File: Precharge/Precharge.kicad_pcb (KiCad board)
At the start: 2 copper layers, 85 x 85 mm, 70 parts, among them J1 Conn_01x02, J2 Conn_01x02, J3 Molex MicroFit, J4 Conn_02x03_Counter_Clockwise, K1 KT12-1A-40L-THT, Q1 CJ2310, Q2 AO3400A, Q3 AO3400A, U1 LM393, U3 4N35, U4 4N35

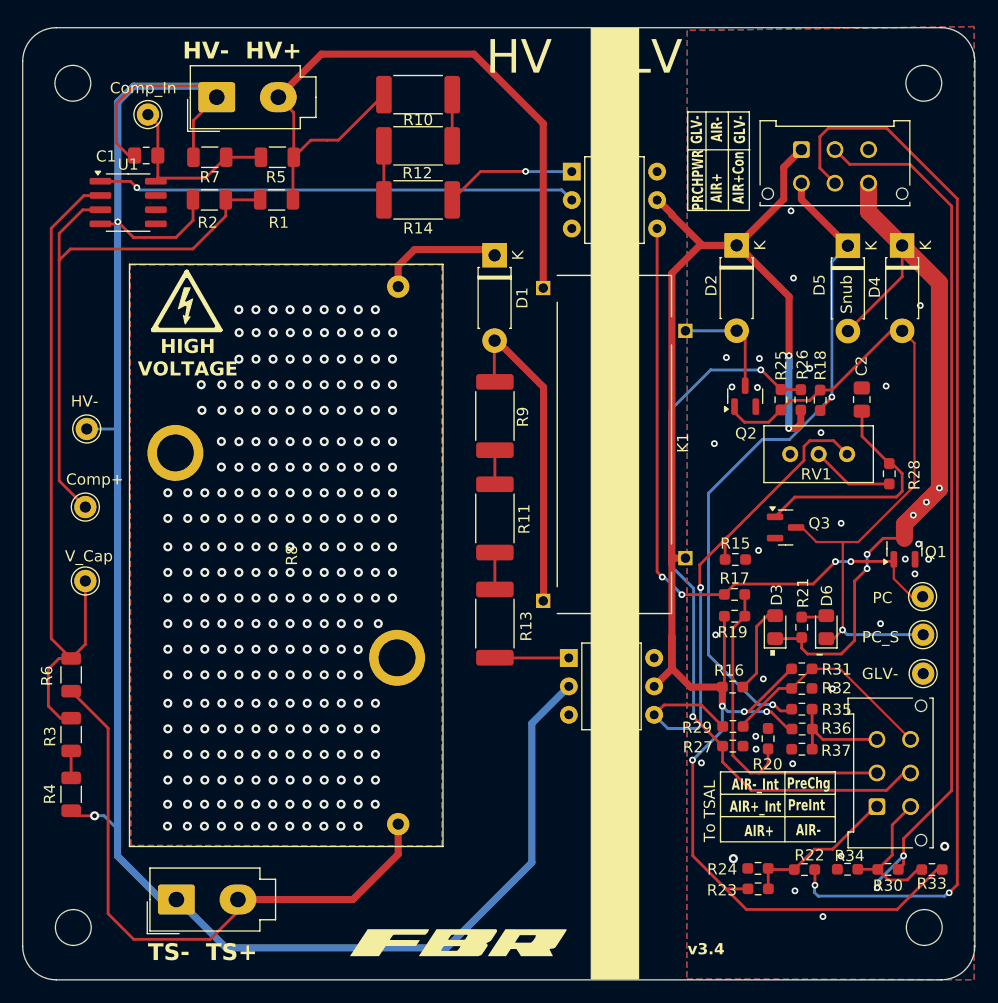
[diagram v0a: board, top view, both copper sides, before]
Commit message: Precharge: Add isolated DC-DC
New Precharge version
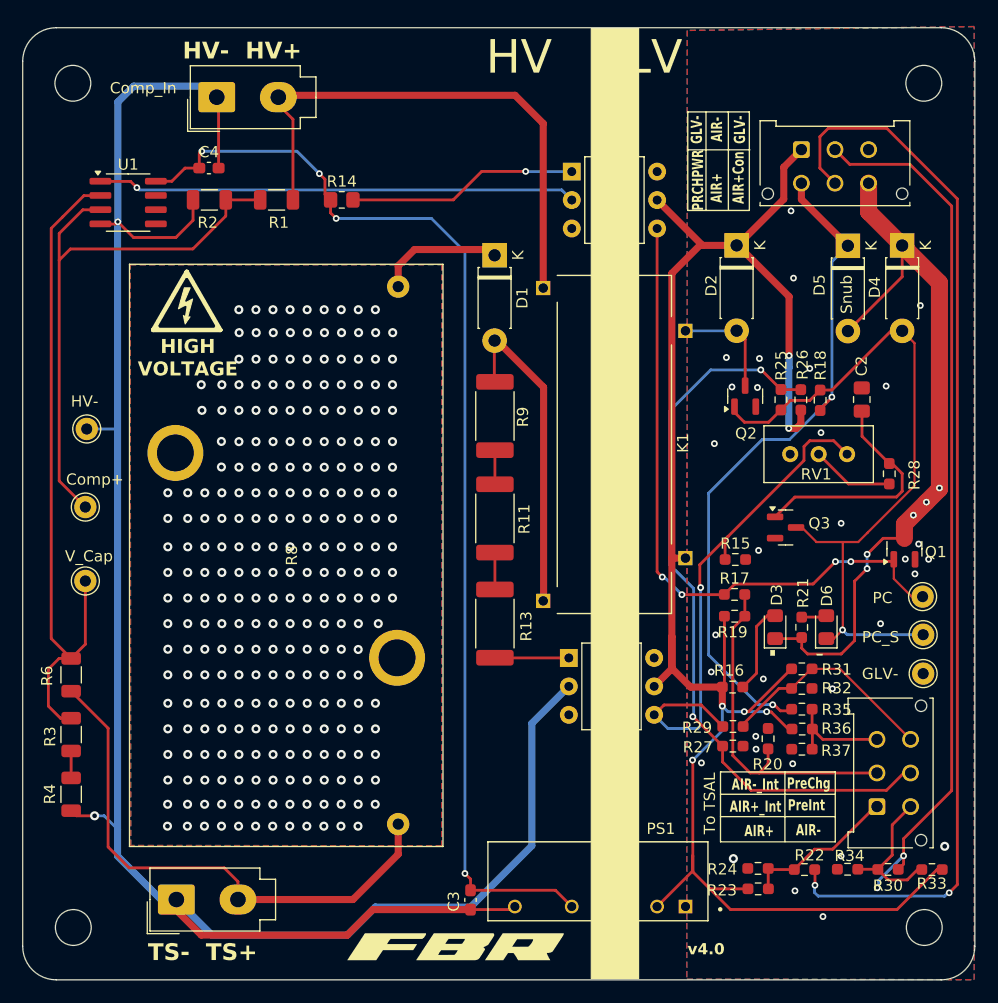
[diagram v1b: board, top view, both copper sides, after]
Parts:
- removed C1: 0.1 uF, Capacitor_SMD:C_0805_2012Metric_Pad1.18x1.45mm_HandSolder
- removed R10, R12: 3.3K, Resistor_SMD:R_2512_6332Metric_Pad1.40x3.35mm_HandSolder
- removed R5: 15K, Resistor_SMD:R_1206_3216Metric
- removed R7: 1.5K, Resistor_SMD:R_1206_3216Metric
- removed TP4: TestPoint, Connector_Pin:Pin_D1.0mm_L10.0mm
- added C3: 0.1uF, Capacitor_SMD:C_0603_1608Metric_Pad1.08x0.95mm_HandSolder, F.Cu at (110.9, 129.6)
- added C4: 0.1uF, Capacitor_SMD:C_0603_1608Metric_Pad1.08x0.95mm_HandSolder, F.Cu at (87.5, 64.2)
- added PS1: RKZE-1205S_HP, Recom DC-DC:CONV_RKZE-1205S_HP, F.Cu at (122.2, 127.9)
- R14: value 3.3K -> 330; footprint Resistor_SMD:R_2512_6332Metric_Pad1.40x3.35mm_HandSolder -> Resistor_SMD:R_0805_2012Metric_Pad1.20x1.40mm_HandSolder
- moved R14 6.82 mm to (99.4, 67.1)
- moved G*** 0.44 mm to (109.4, 133.7)
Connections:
- net /AIR+_GND renamed /AIR-_GND
- net /Comp_Out renamed Net-(U1-Pad1)
- net HV+ renamed TS+
- J3 pad 2: /AIR-_Out -> /AIR+_Out
- J3 pad 5: /AIR+_Out -> /AIR-_Out
- J4 pad 1: /AIR+ -> /AIR-
- J4 pad 2: /AIR+_Int -> /AIR-_Int
- J4 pad 3: /AIR-_Int -> /AIR+_Int
- J4 pad 4: /AIR- -> /AIR+
- R14 pad 1: Net-(R12-Pad2) -> /5V+_Iso
- R17 pad 2: /AIR+_Int -> /AIR-_Int
- R19 pad 2: /AIR+_Int -> /AIR-_Int
- R20 pad 1: /AIR+_Int -> /AIR-_Int
- R22 pad 1: /AIR+_Out -> /AIR-_Out
- R22 pad 2: /AIR+ -> /AIR-
- R23 pad 2: /AIR+ -> /AIR-
- R24 pad 1: /AIR+ -> /AIR-
- R30 pad 1: /AIR-_Out -> /AIR+_Out
- R30 pad 2: /AIR- -> /AIR+
- R33 pad 2: /AIR- -> /AIR+
- R34 pad 1: /AIR- -> /AIR+
- R35 pad 2: /AIR-_Int -> /AIR+_Int
- R36 pad 2: /AIR-_Int -> /AIR+_Int
- R37 pad 1: /AIR-_Int -> /AIR+_Int
- U1 pad 8: Net-(U1C-V+) -> /5V+_Iso
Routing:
- net /5V+_Iso: track 0.00 -> 101.6 mm, vias 0 -> 4
- net /AIR-_Int: track 9.99 -> 30.8 mm
- net /AIR+_Int: track 30.8 -> 9.99 mm
- net /AIR-_Out: track 77.8 -> 96.6 mm
- net /AIR+_Out: track 96.6 -> 77.8 mm
- net HV-: track 179.7 -> 196.4 mm
- net Net-(U1C-V+): track 16.0 -> 0.00 mm
- net TS+: track 63.0 -> 49.5 mm
- net Net-(R14-Pad2): track 11.7 -> 20.6 mm
- net GLV+: track 155.2 -> 163.3 mm
- net Net-(J2-Pin_2): track 54.6 -> 49.5 mm
- net Net-(R12-Pad2): track 4.83 -> 0.00 mm
- net Net-(R10-Pad1): track 4.57 -> 0.00 mm
- net /AIR-: track 13.3 -> 14.1 mm
- net /AIR+: track 14.1 -> 13.3 mm
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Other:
- board text added: "v4.0"
- board text removed: "v3.4"

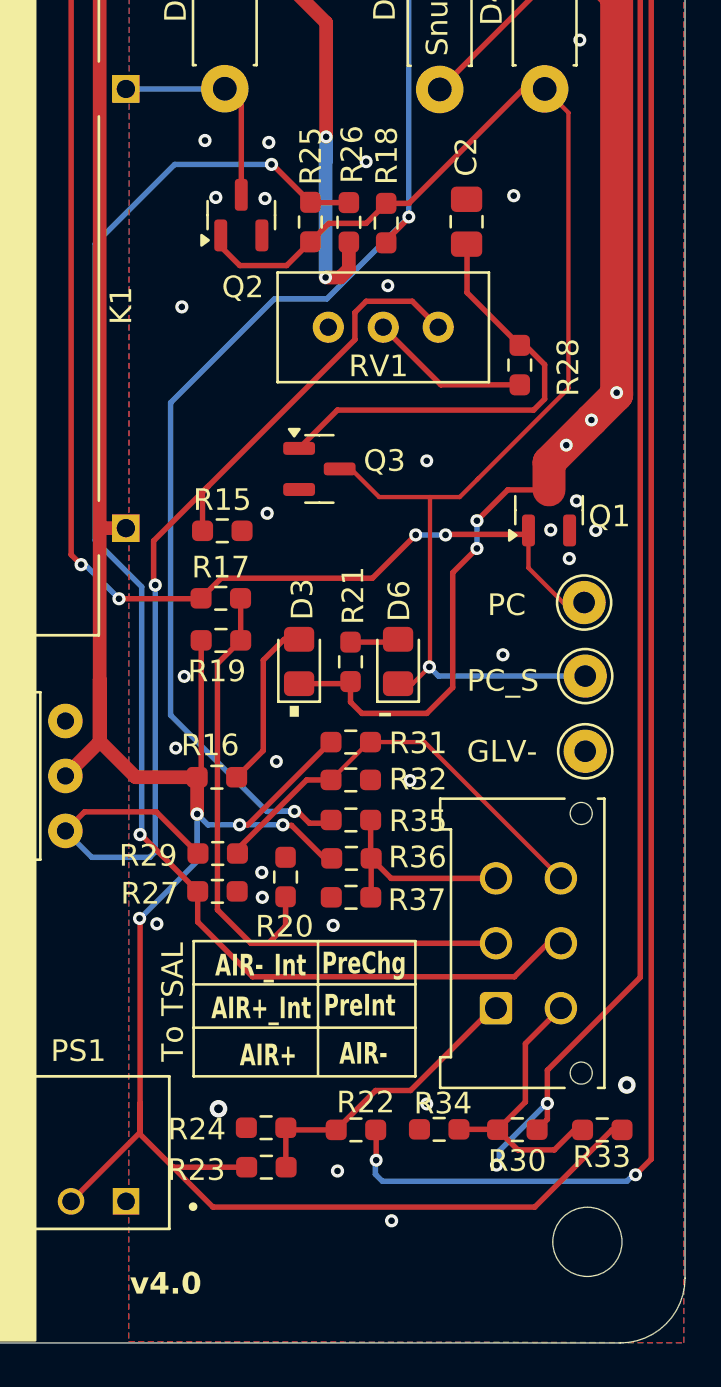
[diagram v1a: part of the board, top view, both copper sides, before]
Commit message: Precharge: cap DC bias correction, PDs on TSAL
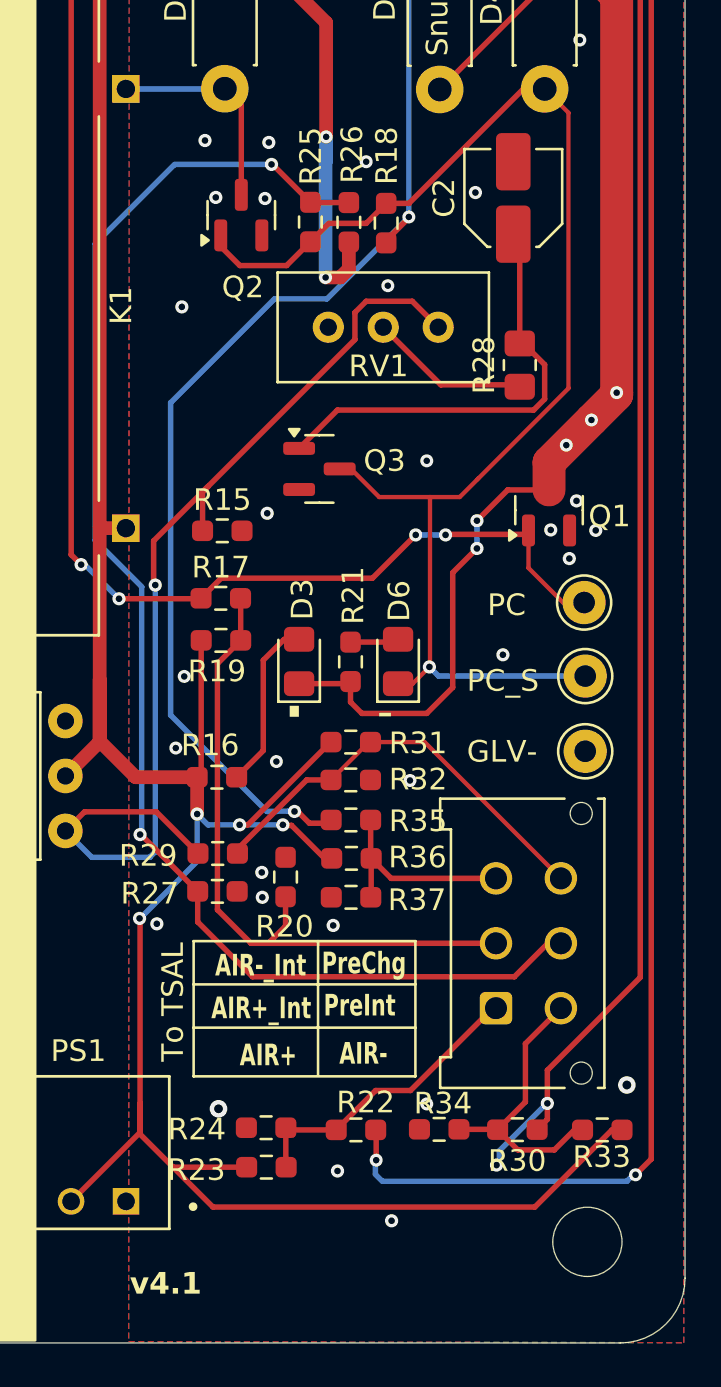
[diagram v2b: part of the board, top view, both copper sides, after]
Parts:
- C2: footprint Capacitor_SMD:C_0805_2012Metric_Pad1.18x1.45mm_HandSolder -> Capacitor_SMD:C_Elec_4x5.4
- R28: footprint Resistor_SMD:R_0603_1608Metric_Pad0.98x0.95mm_HandSolder -> Resistor_SMD:R_0805_2012Metric_Pad1.20x1.40mm_HandSolder
- moved C2 2.42 mm to (148.0, 83.8)
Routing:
- net Net-(Q3-G): track 21.6 -> 20.7 mm
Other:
- board text added: "v4.1"
- board text removed: "v4.0"
